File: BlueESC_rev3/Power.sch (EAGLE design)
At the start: 47 parts, among them Q1 BC817-40W, Q2 BC817-40W, Q3 BC817-40W, Q4 SI7370, Q5 SI7370, Q6 SI7370, Q7 SI7370, Q8 SI7370, Q9 SI7370

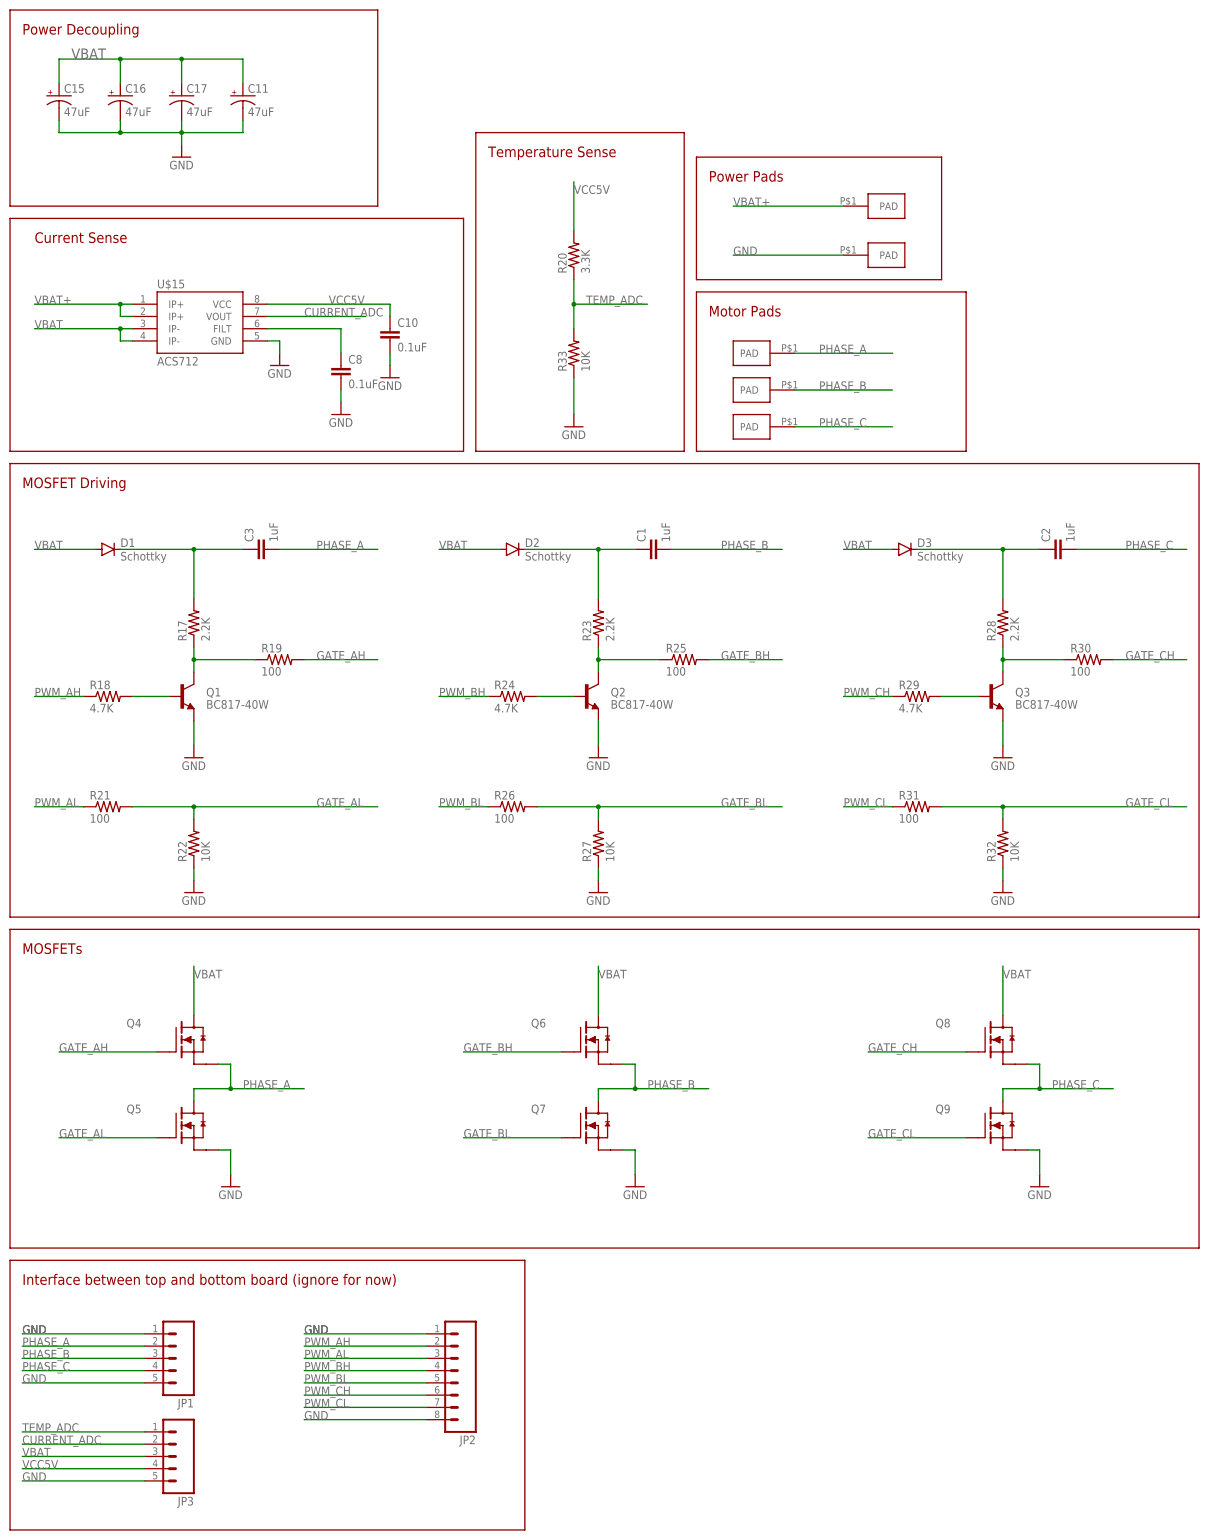
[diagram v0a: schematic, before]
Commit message: Rev3 (two boards) laid out and ready to go. Final review may create a few changes.
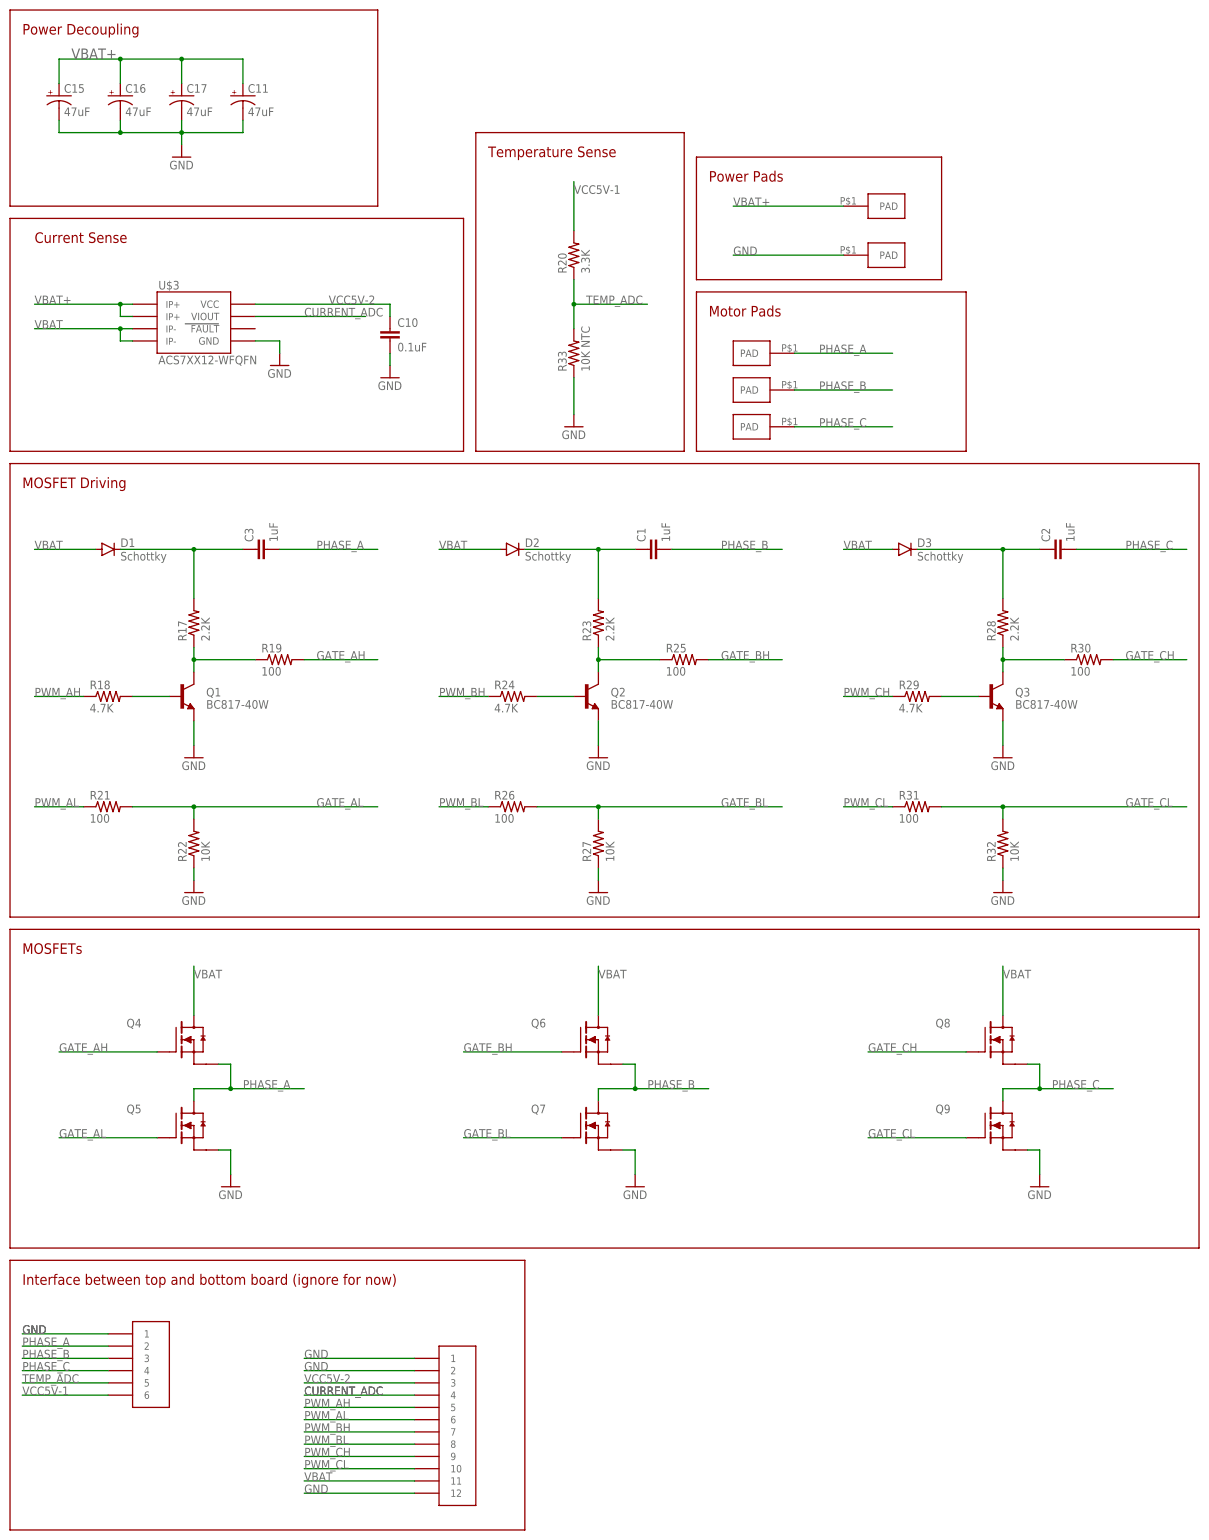
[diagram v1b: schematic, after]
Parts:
- removed C8: 0.1uF, SparkFun-Capacitors:CAP0603-CAP
- removed JP1, JP3: (no value), SparkFun-Connectors:M05PTH
- removed JP2: (no value), SparkFun-Connectors:M081X08
- removed U$15: ACS712, SparkFun-AnalogIC:ACS712
- added U$3: ACS7XX12-WFQFN, BR-Eagle-Library:ACS7XX12-WFQFN
- added U$4: HEADER-62MM, BR-Eagle-Library:HEADER-62MM
- added U$8: HEADER-122MM, BR-Eagle-Library:HEADER-122MM
- R33: value 10K -> 10K NTC
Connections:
- removed net N$1: C8.1, U$15.FILT
- removed net VCC5V: C10.1, JP3.4, R20.2, U$15.VCC
- new net VCC5V-1: R20.2, U$4.6
- new net VCC5V-2: C10.1, U$3.VCC, U$8.3
- net CURRENT_ADC: now also U$3.VIOUT, U$8.4; no longer JP3.2, U$15.VOUT
- net GND: now also U$3.GND, U$4.1, U$8.1, U$8.12, U$8.2; no longer C8.2, JP1.1, JP1.5, JP2.1, JP2.8, JP3.5, U$15.GND
- net PHASE_A: now also U$4.2; no longer JP1.2
- net PHASE_B: now also U$4.3; no longer JP1.3
- net PHASE_C: now also U$4.4; no longer JP1.4
- net PWM_AH: now also U$8.5; no longer JP2.2
- net PWM_AL: now also U$8.6; no longer JP2.3
- net PWM_BH: now also U$8.7; no longer JP2.4
- net PWM_BL: now also U$8.8; no longer JP2.5
- net PWM_CH: now also U$8.9; no longer JP2.6
- net PWM_CL: now also U$8.10; no longer JP2.7
- net TEMP_ADC: now also U$4.5; no longer JP3.1
- net VBAT: now also U$3.IP-1, U$3.IP-2, U$8.11; no longer C11.+, C15.+, C16.+, C17.+, JP3.3, U$15.IP-@3, U$15.IP-@4
- net VBAT+: now also C11.+, C15.+, C16.+, C17.+, U$3.IP+1, U$3.IP+2; no longer U$15.IP+@1, U$15.IP+@2

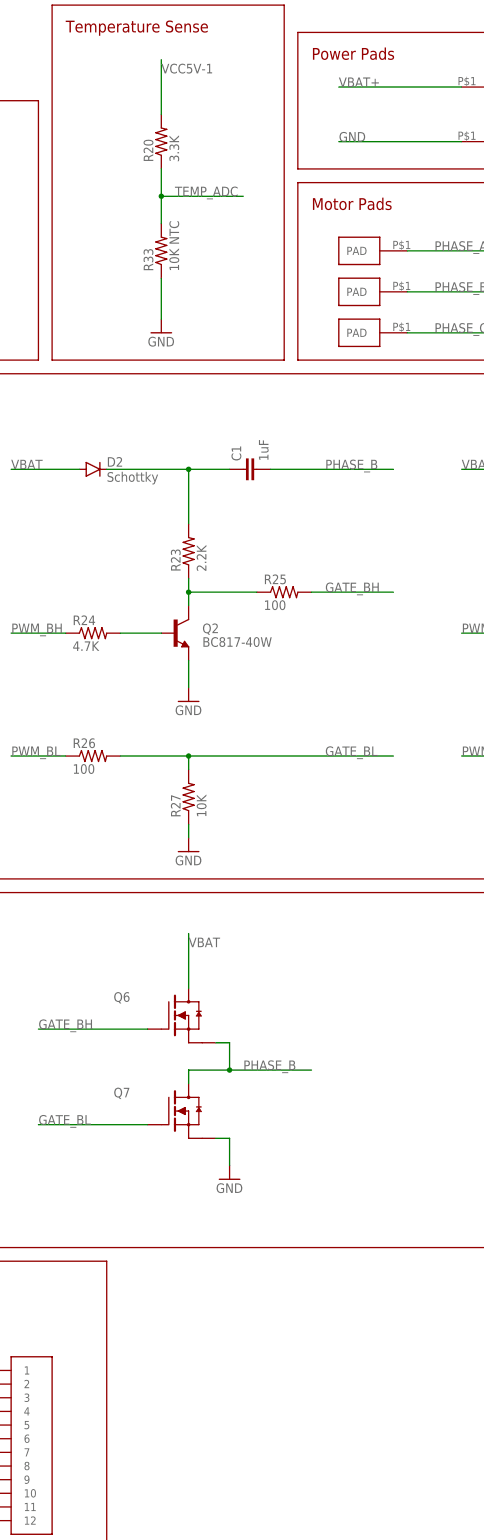
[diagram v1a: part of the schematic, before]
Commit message: Rev 3 changes. Boards have been ordered.
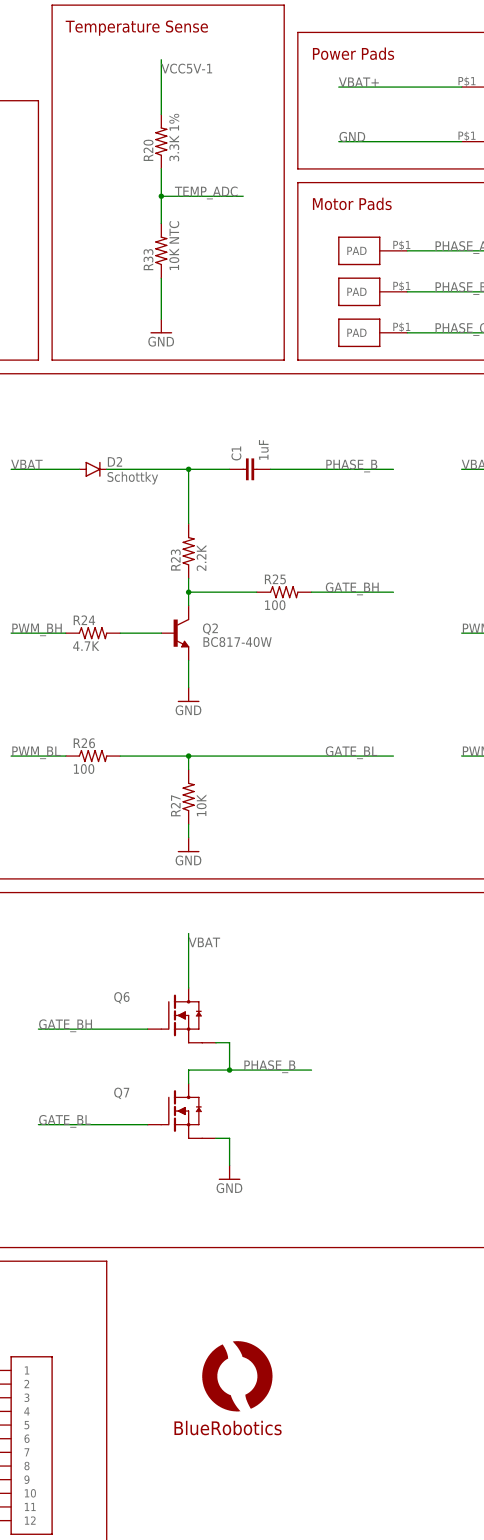
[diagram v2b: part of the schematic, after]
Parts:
- added U$9: LOGOBR-LOGO-S, BR-Eagle-Library:LOGOBR-LOGO-S
- R20: value 3.3K -> 3.3K 1%
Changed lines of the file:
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@@
 <part name="C10" library="SparkFun-Capacitors" deviceset="CAP" device="0603-CAP" value="0.1uF"/>
 <part name="GND17" library="SparkFun-Aesthetics" deviceset="GND" device=""/>
-<part name="R20" library="SparkFun-Resistors" deviceset="33KOHM1/10W1%(0603)" device="" value="3.3K"/>
+<part name="R20" library="SparkFun-Resistors" deviceset="33KOHM1/10W1%(0603)" device="" value="3.3K 1%"/>
 <part name="R33" library="SparkFun-Resistors" deviceset="33KOHM1/10W1%(0603)" device="" value="10K NTC"/>
 <part name="GND23" library="SparkFun-Aesthetics" deviceset="GND" device=""/>
@@
 <part name="U$4" library="BR-Eagle-Library" deviceset="HEADER-6" device="2MM"/>
 <part name="U$8" library="BR-Eagle-Library" deviceset="HEADER-12" device="2MM"/>
+<part name="U$9" library="BR-Eagle-Library" deviceset="LOGO" device="BR-LOGO-S"/>
 </parts>
 <sheets>
@@
 <instance part="U$4" gate="G$1" x="25.4" y="25.4"/>
 <instance part="U$8" gate="G$1" x="88.9" y="5.08"/>
+<instance part="U$9" gate="G$1" x="124.46" y="27.94"/>
 </instances>
 <busses>
